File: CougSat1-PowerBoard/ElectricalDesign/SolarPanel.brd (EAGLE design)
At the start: 79 x 90 mm, 114 parts, among them J1 Wire Harness Connector, U1 SPV1040, U2 SPV1040, U3 TCA9535R, U4 LTC2499, U5 LTC2499, U6 MCP1501-18

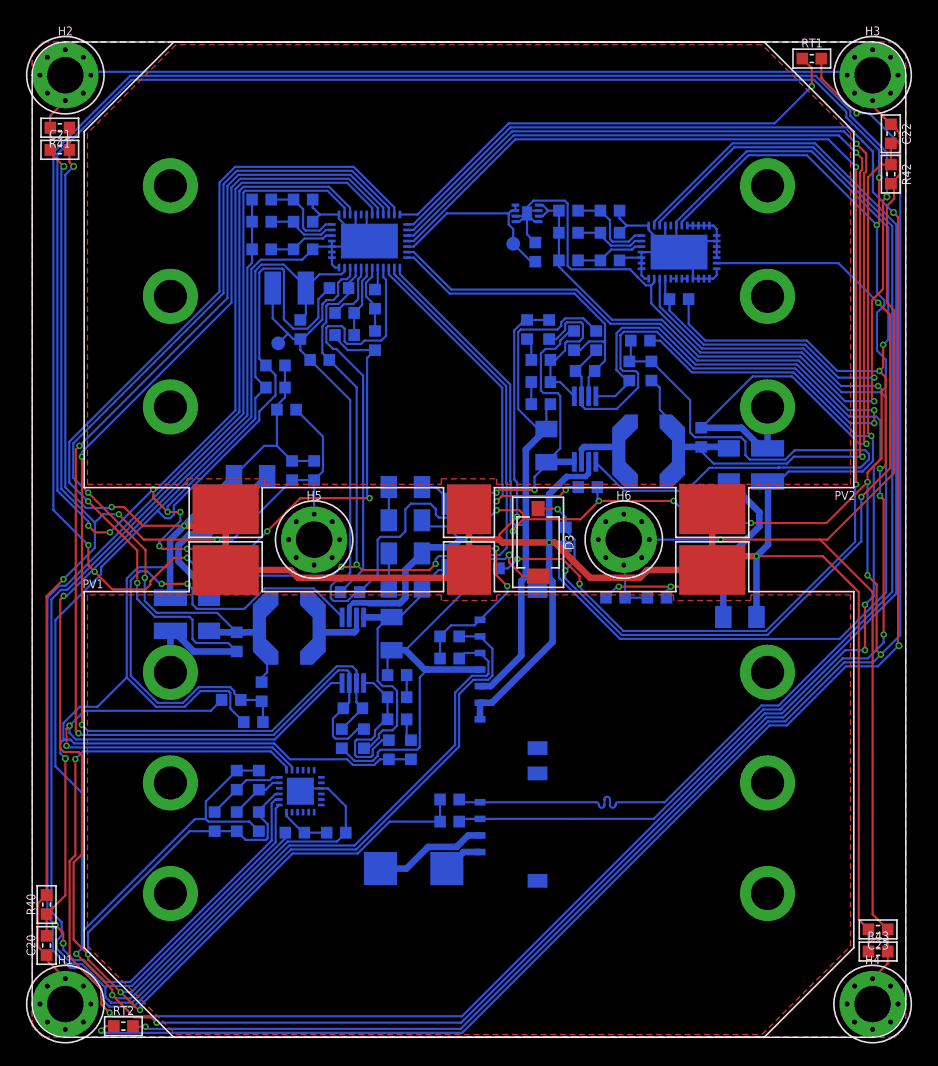
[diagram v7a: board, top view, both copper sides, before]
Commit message: Arranged Reference Designators
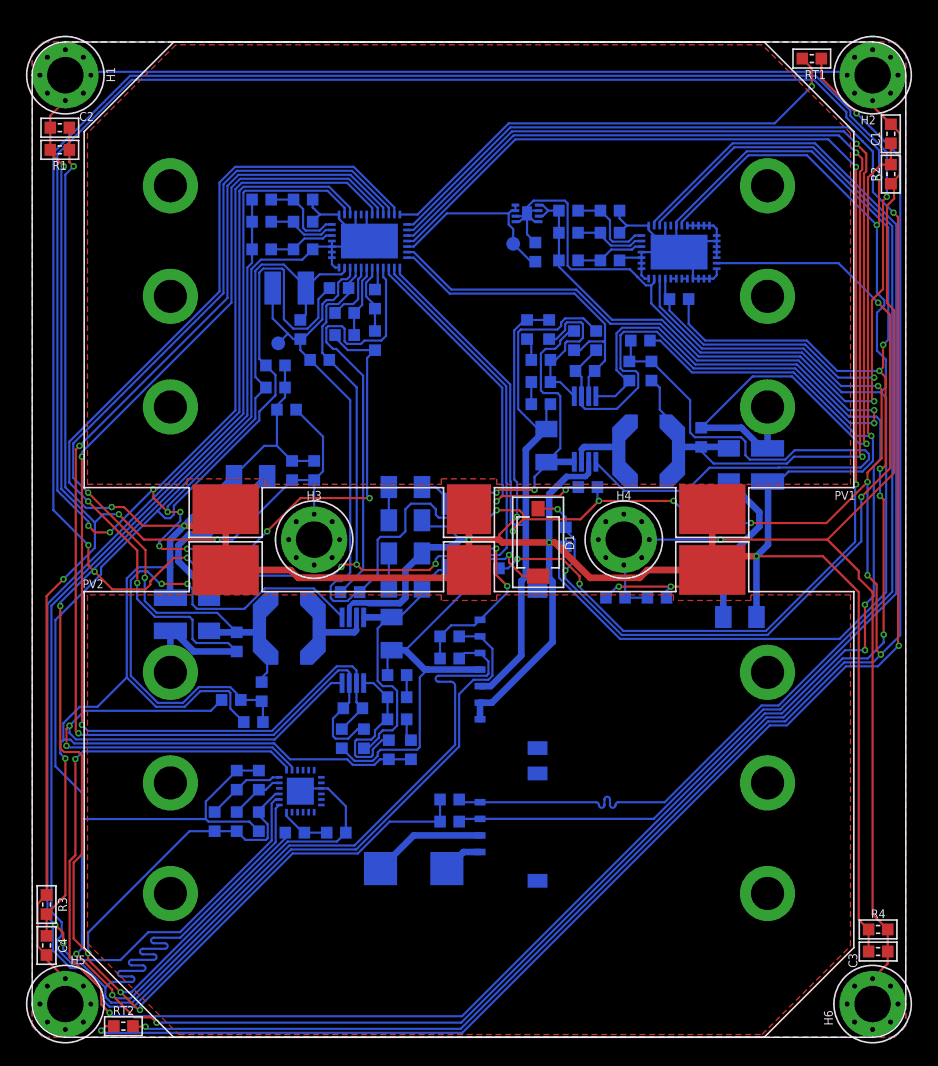
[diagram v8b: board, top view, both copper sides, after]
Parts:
- removed L4: xxx Turns, CougsInSpace-Coils:SMD-3030-2
- added L3: 10µH 20%, CougsInSpace-Coils:6060
- C1: value 47µF -> 100nF 10%; device CougsInSpace-Capacitors:4028-POL -> CougsInSpace-Capacitors:1608
- C10, C17, C20: value 100nF 10% -> 4.7µF 10%; device CougsInSpace-Capacitors:1608 -> CougsInSpace-Capacitors:3216
- C11: value 10µF 10% -> 47µF; device CougsInSpace-Capacitors:3216 -> CougsInSpace-Capacitors:4028-POL
- C12, C5: value 1µF 10% -> 100nF 10%
- C13: value 1nF 10% -> 10µF 10%; device CougsInSpace-Capacitors:1608 -> CougsInSpace-Capacitors:3216
- C15: value 270pF 1% -> 10µF 10%; device CougsInSpace-Capacitors:1608 -> CougsInSpace-Capacitors:3216
- C16: value 100nF 10% -> 10µF 10%; device CougsInSpace-Capacitors:1608 -> CougsInSpace-Capacitors:3216
- C18: value 4.7µF 10% -> 100nF 10%; device CougsInSpace-Capacitors:4028-POL -> CougsInSpace-Capacitors:1608
- C19: value 100nF 10% -> 47µF; device CougsInSpace-Capacitors:1608 -> CougsInSpace-Capacitors:4028-POL
- C2: value 4.7µF 10% -> 100nF 10%; device CougsInSpace-Capacitors:3216 -> CougsInSpace-Capacitors:1608
- C21: value 100nF 10% -> 1µF 10%
- C23: value 100nF 10% -> 1nF 10%
- C27: device CougsInSpace-Capacitors:3216 -> CougsInSpace-Capacitors:4028-POL
- C28: value 4.7µF 10% -> 270pF 1%; device CougsInSpace-Capacitors:3216 -> CougsInSpace-Capacitors:1608
- C4, C7: value 10µF 10% -> 100nF 10%; device CougsInSpace-Capacitors:3216 -> CougsInSpace-Capacitors:1608
- C8: value 47µF -> 1µF 10%; device CougsInSpace-Capacitors:4028-POL -> CougsInSpace-Capacitors:1608
- D1: value SMM4F5.0A -> SFH 2430; device CougsInSpace-DiscreteSemi:STMITE -> CougsInSpace-Sensors:SFH2430
- D3: value SFH 2430 -> SMM4F5.0A; device CougsInSpace-Sensors:SFH2430 -> CougsInSpace-DiscreteSemi:STMITE
- J1: value Wire Harness Connector -> (none); device CougsInSpace-Connectors:PICOLOCK1.5-07 -> CougsInSpace-Connectors:PICOLOCK1.5-04
- J2: value (none) -> Wire Harness Connector; device CougsInSpace-Connectors:PICOLOCK1.5-04 -> CougsInSpace-Connectors:PICOLOCK1.5-07
- L1: value 10µH 20% -> xxx Turns; device CougsInSpace-Coils:6060 -> CougsInSpace-Coils:SMD-3030-2
- R1, R11, R4, R5: value 1kΩ 0.1% -> 0Ω <20mΩ
- R12, R2: value 10kΩ 0.1% -> 0Ω <20mΩ
- R13, R42: value 0Ω <20mΩ -> 360kΩ 1%
- R16, R6: value 820kΩ 1% -> 0Ω <20mΩ
- R17: value 360kΩ 1% -> 10kΩ 0.1%
- R18: value 50mΩ 1% -> 820kΩ 1%
- R19, R34, R39: value 0Ω <20mΩ -> 1kΩ 0.1%
- R22, R29: value 0Ω <20mΩ -> 50mΩ 1%
- R24, R28: value 0Ω <20mΩ -> 100mΩ 1%; device CougsInSpace-Resistors:1608 -> CougsInSpace-Resistors:3216
- R26: value 0Ω <20mΩ -> 150Ω 1%
- R33: value 0Ω <20mΩ -> 820kΩ 1%
- R35: value 33kΩ 1% -> 10kΩ 0.1%
- R36: value 33kΩ 1% -> 0Ω <20mΩ
- R37: value 8.45kΩ 0.1% -> 0Ω <20mΩ
- R38: value 8.45kΩ 0.1% -> 1kΩ 0.1%
- R40, R41: value 0Ω <20mΩ -> 8.45kΩ 0.1%
- R43, R44: value 0Ω <20mΩ -> 33kΩ 1%
- R46, R47: value 100mΩ 1% -> 0Ω <20mΩ; device CougsInSpace-Resistors:3216 -> CougsInSpace-Resistors:1608
- R56: value 150Ω 1% -> 0Ω <20mΩ
- R7: value 360kΩ 1% -> 0Ω <20mΩ
- R8: value 50mΩ 1% -> 0Ω <20mΩ
- U1: value SPV1040 -> TCA9535R; device CougsInSpace-IC-Power:TSSOP8 -> CougsInSpace-IC-Conversion:QFN-24-4040
- U3: value TCA9535R -> SPV1040; device CougsInSpace-IC-Conversion:QFN-24-4040 -> CougsInSpace-IC-Power:TSSOP8
- moved H1 84.0 mm to (-36.5, 42.0)
- moved C1 78.3 mm to (38.1, 36.7), flipped to the top
- moved R2 76.3 mm to (38.1, 33.0), flipped to the top, turned to 270 degrees
- moved C20 75.5 mm to (23.5, 6.75), flipped to the bottom, turned to 270 degrees
- moved R43 75.3 mm to (-11.2, 20.5), flipped to the bottom
- moved H2 73.0 mm to (36.5, 42.0)
- moved H3 65.7 mm to (-14.0, 0.00)
- moved C23 61.9 mm to (7.25, 19.0), flipped to the bottom, turned to 90 degrees
- moved C3 59.5 mm to (37.0, -35.2), flipped to the top, turned to 180 degrees
- moved R40 59.0 mm to (-8.50, 18.0), flipped to the bottom
- moved R54 56.3 mm to (9.00, 29.8)
- moved R55 55.8 mm to (-15.0, 30.8)
- moved R29 54.5 mm to (21.0, 9.25)
- moved R1 54.2 mm to (-37.0, 37.2), flipped to the top, turned to 180 degrees
- moved C21 51.5 mm to (10.5, 15.2), flipped to the bottom
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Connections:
- net !MPPT_XSHUT-A: now also R17.2, U1.2, U2.8; no longer R2.2, U1.8, U3.2
- net !MPPT_XSHUT-B: now also R35.2, U1.1, U3.8; no longer R12.2, U2.8, U3.1
- net 3.3V: now also C25.1, C5.1, J2.1, R10.2, R46.2, R52.2, R56.2, R6.2, R7.2, R8.2, R9.2, U1.21; no longer C16.1, C17.1, J1.1, R13.2, R22.2, R28.2, R29.2, R3.2, R30.2, R49.2, R55.2, U3.21
- net ADC_ADCS_CA0: now also R45.2, R46.1, U4.36; no longer R48.1, R51.2, U5.36
- net ADC_ADCS_CA1: now also R49.2, R50.1, U4.37; no longer R49.1, R52.2, U5.37
- net ADC_ADCS_CA2: now also R54.1, U4.38; no longer R50.1, U5.38
- net ADC_ADCS_MUXOUTN: now also U4.26, U4.27; no longer U5.26, U5.27
- net ADC_ADCS_MUXOUTP: now also U4.24, U4.25; no longer U5.24, U5.25
- net ADC_EPS-MUXOUTN: now also R43.2, U5.27; no longer R35.2, U4.27
- net ADC_EPS_ADCINN: now also R41.2, R43.1, U5.26; no longer R35.1, R37.2, U4.26
- net ADC_EPS_ADCINP: now also R40.2, R44.1, U5.25; no longer R36.1, R38.2, U4.25
- net ADC_EPS_CA0: now also R47.2, R48.1, U5.36; no longer R21.1, R24.2, U4.36
- net ADC_EPS_CA1: now also R51.2, R52.1, U5.37; no longer R22.1, R25.2, U4.37
- net ADC_EPS_CA2: now also R55.2, R56.1, U5.38; no longer R23.1, R26.2, U4.38
- net ADC_EPS_MUXOUTP: now also R44.2, U5.24; no longer R36.2, U4.24
- net AGND: now also C24.2, C27.C, C28.2, R26.1, R32.1, R40.1, R41.1; no longer C15.2, C18.C, C19.2, R33.1, R37.1, R38.1, R56.1
- net AVDD: now also C24.1, C27.A, D1.C, RT3.1, RT4.2, TP1.1; no longer C18.A, C19.1, D3.C, RT3.2, RT4.1, TP2.1
- net AVREF: now also C28.1, TP2.1, U5.17; no longer C15.1, TP1.1, U4.17
- net CHASSIS: now also C1.1, C12.1, C18.1, C2.1, C3.1, C4.1, R1.2, R2.2, R25.2, R27.2, R3.2, R30.1, R4.2; no longer C20.1, C21.1, C22.1, C23.1, C24.1, C25.1, R39.1, R40.2, R41.2, R42.2, R43.2, R44.2, R45.2
- net DGND: now also C25.2, C5.2, R11.1, R12.1, R36.1, R45.1, R47.1, R49.1, R5.1, R55.1, U1.9, U1.PAD, U4.10, U4.11, U4.12, U4.13, U4.14, U4.15, U4.16, U4.17, U4.19, U4.20, U4.21, U4.22, U4.23, U4.8, U4.9; no longer C16.2, C17.2, R24.1, R25.1, R26.1, R27.1, R31.1, R32.1, R34.1, R52.1, U3.9, U3.PAD, U5.10, U5.11, U5.12, U5.13, U5.14, U5.15, U5.16, U5.17, U5.19, U5.20, U5.21, U5.22, U5.23, U5.8, U5.9
- net GPIO_A0: now also R5.2, R6.1, U1.18; no longer R30.1, R34.2, U3.18
- net GPIO_A1: now also R11.2, R8.1, U1.23; no longer R29.1, R32.2, U3.23
- net GPIO_A2: now also R12.2, R9.1, U1.24; no longer R28.1, R31.2, U3.24
- net I2C_SCL_ADCS: now also J1.2, R7.1, U4.2; no longer J2.2, R54.1, U5.2
- net I2C_SCL_PMIC: now also J2.3, R21.1, U1.19, U5.2; no longer J1.3, R3.1, U3.19, U4.2
- net I2C_SDA_ADCS: now also J1.1, R10.1, U4.3; no longer J2.1, R55.1, U5.3
- net I2C_SDA_PMIC: now also J2.2, R23.1, U1.20, U5.3; no longer J1.2, R13.1, U3.20, U4.3
- net MAGNETORQUER-IN: now also J1.3, L1.1; no longer J2.3, L4.1
- net MAGNETORQUER_OUT: now also J1.4, L1.2; no longer J2.4, L4.2
- net MPPT_FBRES_HIGH-A: now also R18.2, R20.1; no longer R6.2, R9.1
- net MPPT_FBRES_HIGH-B: now also R31.1, R33.2; no longer R16.2, R19.1
- net MPPT_FBRES_LOW-A: now also R13.2, R16.1; no longer R10.1, R7.2
- net MPPT_FBRES_LOW-B: now also R37.1, R42.2; no longer R17.2, R20.1
- net MPPT_ICTRL_N-A: now also C8.2, R15.1, U2.6, U5.8; no longer C5.2, R5.1, U1.6, U4.8
- net MPPT_ICTRL_N-B: now also C21.2, R38.1, U3.6, U5.18; no longer C12.2, R15.1, U2.6, U4.18
- net MPPT_ICTRL_P-A: now also C8.1, R14.1, U2.7, U5.9; no longer C5.1, R4.1, U1.7, U4.9
- net MPPT_ICTRL_P-B: now also C21.1, R39.1, U3.7, U5.19; no longer C12.1, R14.1, U2.7, U4.19
- net MPPT_LX-A: now also L2.2, U2.3; no longer L1.2, U1.3
- net MPPT_LX-B: now also L3.2, U3.3; no longer L2.2, U2.3
- net MPPT_OUTCAP-A: now also C13.2, C14.1; no longer C4.2, C7.1
- net MPPT_OUTCAP-B: now also C15.1, C16.2; no longer C11.2, C14.1
- net MPPT_SET-A: now also C7.1, R17.1, R19.1, U2.1; no longer C3.1, R1.1, R2.1, U1.1
- net MPPT_SET-B: now also C22.1, R34.1, R35.1, U3.1; no longer C10.1, R11.1, R12.1, U2.1
- net MPPT_VCTRL-A: now also R16.2, R18.1, U2.5; no longer R10.2, R6.1, U1.5
- net MPPT_VCTRL-B: now also C23.1, R33.1, R37.2, U3.5; no longer C13.1, R16.1, R20.2, U2.5
- net MPPT_VOUT-A: now also C13.1, R14.2, R24.1, U2.4; no longer C4.1, R4.2, R46.1, U1.4
- net MPPT_VOUT-B: now also C16.1, D3.C, R28.1, R39.2, U3.4; no longer C11.1, D1.C, R14.2, R47.1, U2.4
- net OUTPUT_CAP-A: now also C10.2, C17.1; no longer C2.2, C27.1
- net OUTPUT_CAP-B: now also C20.2, C9.1; no longer C28.1, C9.2
- net PGND: now also C1.2, C11.C, C12.2, C15.2, C17.2, C18.2, C19.C, C2.2, C4.2, C9.2, D3.A, J2.6, J2.7, R1.1, R13.1, R2.1, R25.1, R27.1, R3.1, R30.2, R32.2, R36.2, R4.1, U3.2; no longer C1.C, C10.2, C13.2, C20.2, C21.2, C24.2, C25.2, C27.2, C28.2, C8.C, D1.A, J1.6, J1.7, R17.1, R27.2, R33.2, R39.2, R40.1, R41.1, R43.1, R44.1, R45.1, R7.1, U1.2
- net PHOTODIODE: now also D1.A, R26.2, U4.18; no longer D3.A, R56.2, U5.18
- net PV_IIN_N-A: now also C10.1, L2.1, R19.2, R22.2, U5.10; no longer C2.1, L1.1, R1.2, R8.2, U4.10
- net PV_IIN_N-B: now also C20.1, L3.1, R29.2, R34.2, U5.15; no longer C9.1, L2.1, R11.2, R18.2, U4.15
- net PV_IIN_P-A: now also C11.A, PV2.VCC@1, PV2.VCC@2, PV2.VCC@3, PV2.VCC@4, PV2.VCC@5, PV2.VCC@6, R22.1, U5.11; no longer C1.A, PV1.VCC@1, PV1.VCC@2, PV1.VCC@3, PV1.VCC@4, PV1.VCC@5, PV1.VCC@6, R8.1, U4.11
- net PV_IIN_P-B: now also C19.A, PV1.VCC@1, PV1.VCC@2, PV1.VCC@3, PV1.VCC@4, PV1.VCC@5, PV1.VCC@6, R29.1, U5.14; no longer C8.A, PV2.VCC@1, PV2.VCC@2, PV2.VCC@3, PV2.VCC@4, PV2.VCC@5, PV2.VCC@6, R18.1, U4.14
- net TEMP_BACK: now also RT4.1, U5.16; no longer RT3.1, U4.16
- net TEMP_FRONT_BOTTOM: now also U5.12; no longer U4.12
- net TEMP_FRONT_TOP: now also U5.13; no longer U4.13
- net TEMP_MPPT-A: now also RT3.2, U5.23; no longer RT5.2, U4.23
- net TEMP_MPPT-B: now also RT5.2, U5.22; no longer RT4.2, U4.22
- net VOUT-A: now also J2.4, R15.2, R20.2, R24.2, U5.21; no longer J1.4, R46.2, R5.2, R9.2, U4.21
- net VOUT-B: now also J2.5, R28.2, R31.2, R38.2, U5.20; no longer J1.5, R15.2, R19.2, R47.2, U4.20
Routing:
- net I2C_SCL_PMIC: track 172.2 -> 185.9 mm
- net DGND: track 414.4 -> 410.1 mm
- net I2C_SDA_PMIC: track 183.7 -> 181.7 mm
- net AVDD: track 306.6 -> 304.8 mm
